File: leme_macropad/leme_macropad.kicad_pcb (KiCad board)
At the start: 4 copper layers, 99.9 x 63.9 mm, 90 parts, among them J1 OLED display, J2 USB_C_Receptacle_USB2.0_16P, SW1 SW_Push, SW2 SW_Push, SW3 SW_Push, SW4 RotaryEncoder_Switch, SW5 SW_Push, SW6 SW_Push, SW7 SW_Push, SW8 SW_Push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

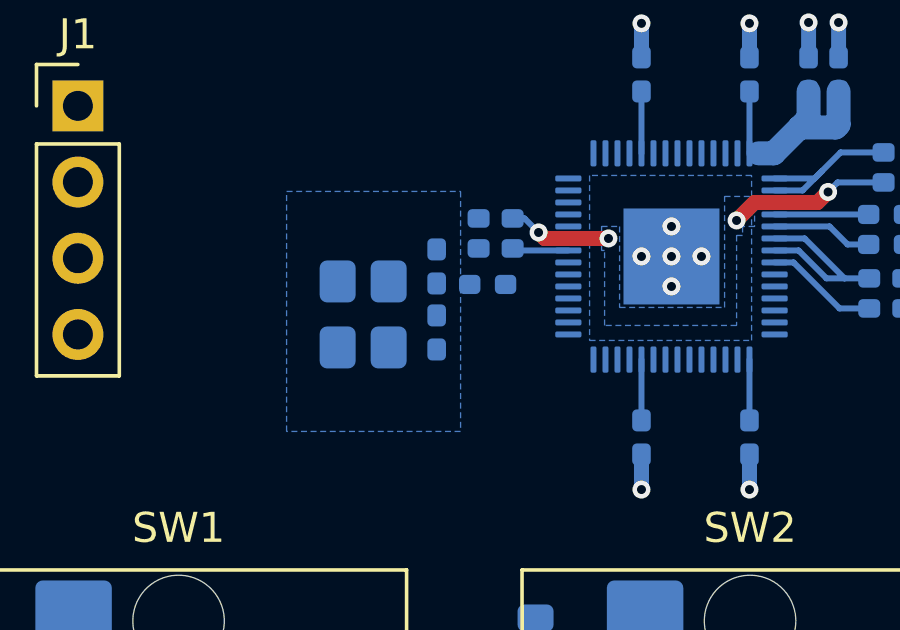
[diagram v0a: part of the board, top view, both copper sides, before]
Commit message: Routes crystal oscillator
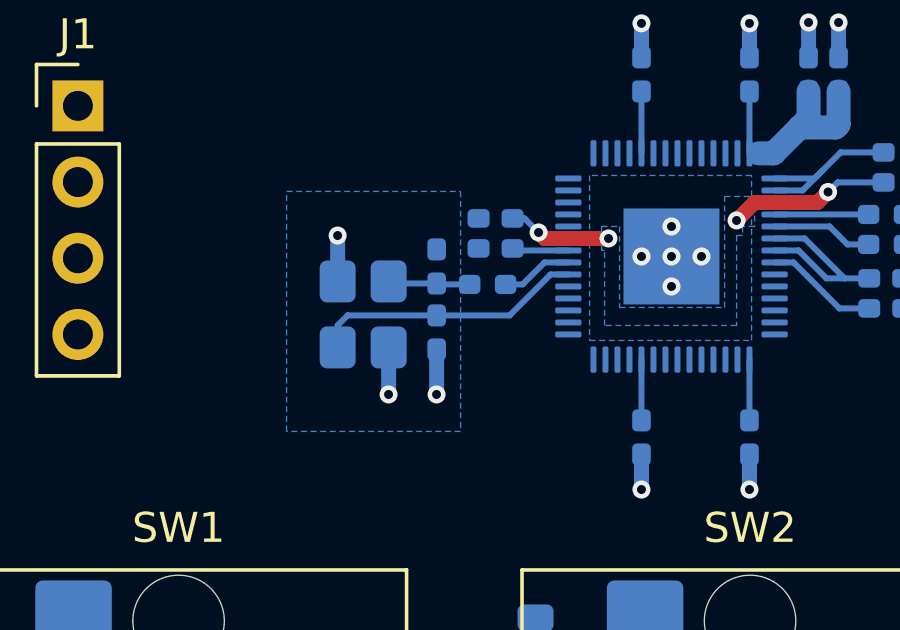
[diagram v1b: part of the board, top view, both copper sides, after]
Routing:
- net XIN: track 0.00 -> 9.13 mm
- net GND: track 12.8 -> 17.4 mm, vias 15 -> 18
- net Net-(C7-Pad2): track 0.00 -> 2.74 mm
- net XOUT: track 0.00 -> 2.40 mm
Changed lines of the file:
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@@
+	)
+	(via
+		(at 127.6 80)
+		(size 0.6)
+		(drill 0.3)
+		(layers "F.Cu" "B.Cu")
+		(net 2)
 	)
 	(via
@@
 	)
 	(via
+		(at 126 80)
+		(size 0.6)
+		(drill 0.3)
+		(layers "F.Cu" "B.Cu")
+		(net 2)
+	)
+	(via
+		(at 124.3025 74.7025)
+		(size 0.6)
+		(drill 0.3)
+		(layers "F.Cu" "B.Cu")
+		(net 2)
+	)
+	(via
 		(at 138.03 67.63)
 		(size 0.6)
@@
 		(drill 0.3)
 		(layers "F.Cu" "B.Cu")
+		(net 2)
+	)
+	(segment
+		(start 126.0025 79.9975)
+		(end 126 80)
+		(width 0.5)
+		(layer "B.Cu")
 		(net 2)
 	)
@@
 	)
 	(segment
+		(start 127.6025 79.9975)
+		(end 127.6 80)
+		(width 0.5)
+		(layer "B.Cu")
+		(net 2)
+	)
+	(segment
+		(start 126.0025 78.4325)
+		(end 126.0025 79.9975)
+		(width 0.5)
+		(layer "B.Cu")
+		(net 2)
+	)
+	(segment
 		(start 134.43 67.63)
 		(end 134.43 68.765)
@@
 	)
 	(segment
+		(start 124.3025 74.7025)
+		(end 124.3025 76.2325)
+		(width 0.5)
+		(layer "B.Cu")
+		(net 2)
+	)
+	(segment
 		(start 144.6 77.1325)
 		(end 143.157144 77.1325)
+		(width 0.5)
+		(layer "B.Cu")
+		(net 2)
+	)
+	(segment
+		(start 127.6025 78.5)
+		(end 127.6025 79.9975)
 		(width 0.5)
 		(layer "B.Cu")
@@
 	)
 	(segment
+		(start 124.635 77.365)
+		(end 127.6025 77.365)
+		(width 0.2)
+		(layer "B.Cu")
+		(net 4)
+	)
+	(segment
+		(start 131.4 76)
+		(end 131.9925 76)
+		(width 0.2)
+		(layer "B.Cu")
+		(net 4)
+	)
+	(segment
+		(start 127.6025 77.365)
+		(end 130.035 77.365)
+		(width 0.2)
+		(layer "B.Cu")
+		(net 4)
+	)
+	(segment
+		(start 124.3025 78.4325)
+		(end 124.3025 77.6975)
+		(width 0.2)
+		(layer "B.Cu")
+		(net 4)
+	)
+	(segment
+		(start 124.3025 77.6975)
+		(end 124.635 77.365)
+		(width 0.2)
+		(layer "B.Cu")
+		(net 4)
+	)
+	(segment
+		(start 130.035 77.365)
+		(end 131.4 76)
+		(width 0.2)
+		(layer "B.Cu")
+		(net 4)
+	)
+	(segment
+		(start 127.6025 76.3)
+		(end 126.07 76.3)
+		(width 0.2)
+		(layer "B.Cu")
+		(net 5)
+	)
+	(segment
+		(start 127.635 76.3325)
+		(end 127.6025 76.3)
+		(width 0.2)
+		(layer "B.Cu")
+		(net 5)
+	)
+	(segment
+		(start 126.07 76.3)
+		(end 126.0025 76.2325)
+		(width 0.2)
+		(layer "B.Cu")
+		(net 5)
+	)
+	(segment
+		(start 128.705 76.3325)
+		(end 127.635 76.3325)
+		(width 0.2)
+		(layer "B.Cu")
+		(net 5)
+	)
+	(segment
 		(start 140.65 73.25)
 		(end 140.3 73.6)
@@
 	)
 	(segment
+		(start 130.4675 76.3325)
+		(end 129.9 76.3325)
+		(width 0.2)
+		(layer "B.Cu")
+		(net 33)
+	)
+	(segment
+		(start 131.9925 75.6)
+		(end 131.2 75.6)
+		(width 0.2)
+		(layer "B.Cu")
+		(net 33)
+	)
+	(segment
+		(start 131.2 75.6)
+		(end 130.4675 76.3325)
+		(width 0.2)
+		(layer "B.Cu")
+		(net 33)
+	)
+	(segment

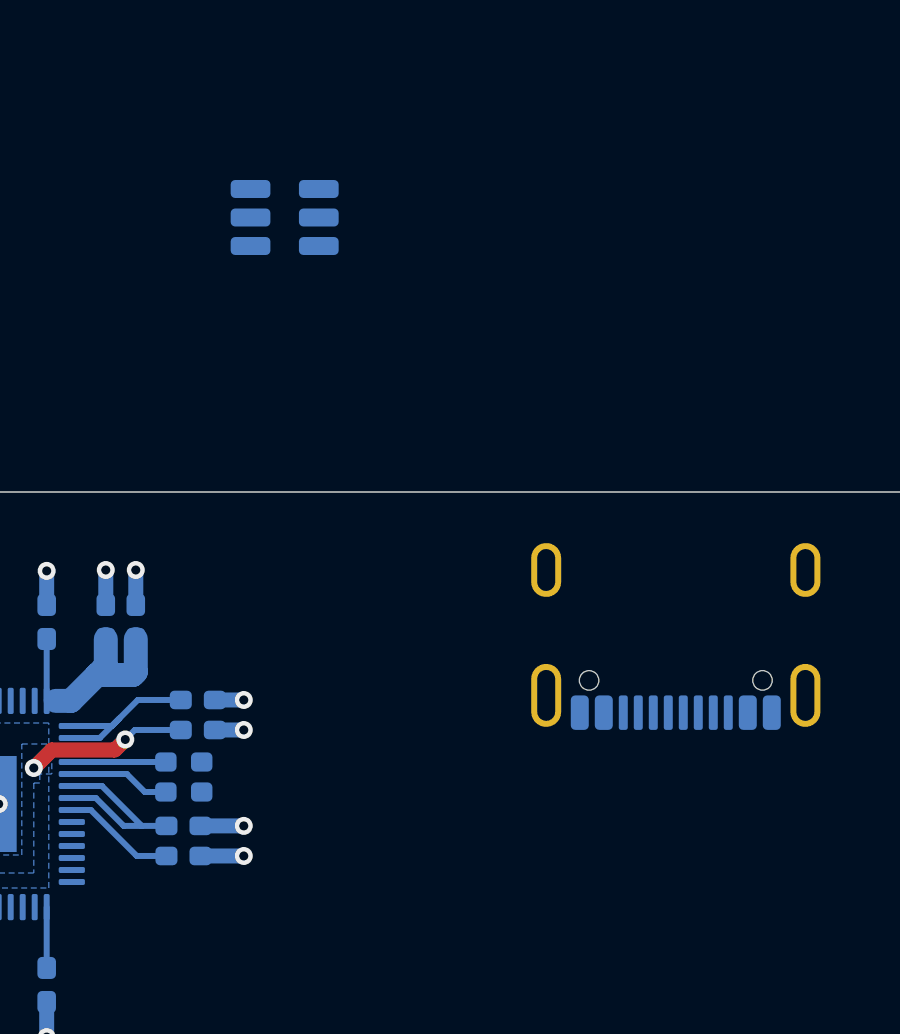
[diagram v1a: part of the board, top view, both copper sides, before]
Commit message: Routes USB diffpair
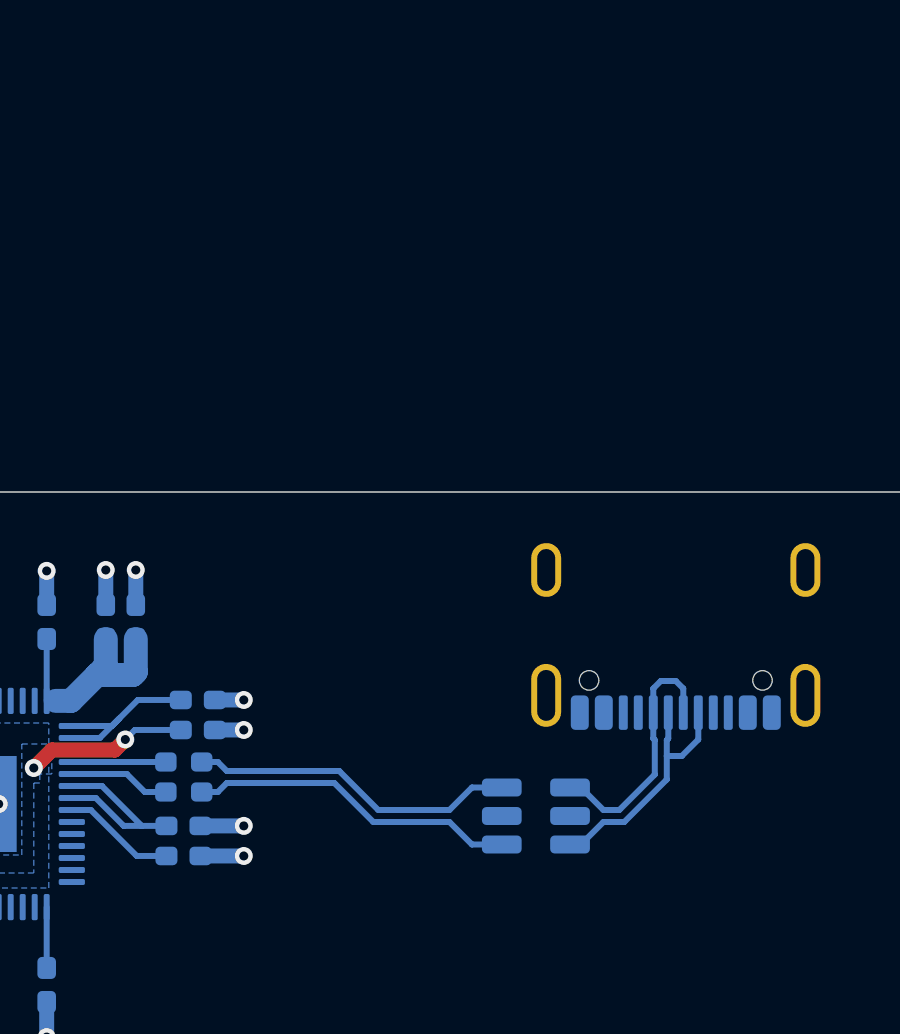
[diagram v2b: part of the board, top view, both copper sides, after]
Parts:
- moved U1 21.6 mm to (154.3, 75.8), turned to 180 degrees
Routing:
- net USB_D-: track 0.00 -> 11.0 mm
- net USB_D+: track 0.00 -> 11.0 mm
- net /conn_D+: track 0.00 -> 8.54 mm
- net /conn_D-: track 0.00 -> 8.53 mm

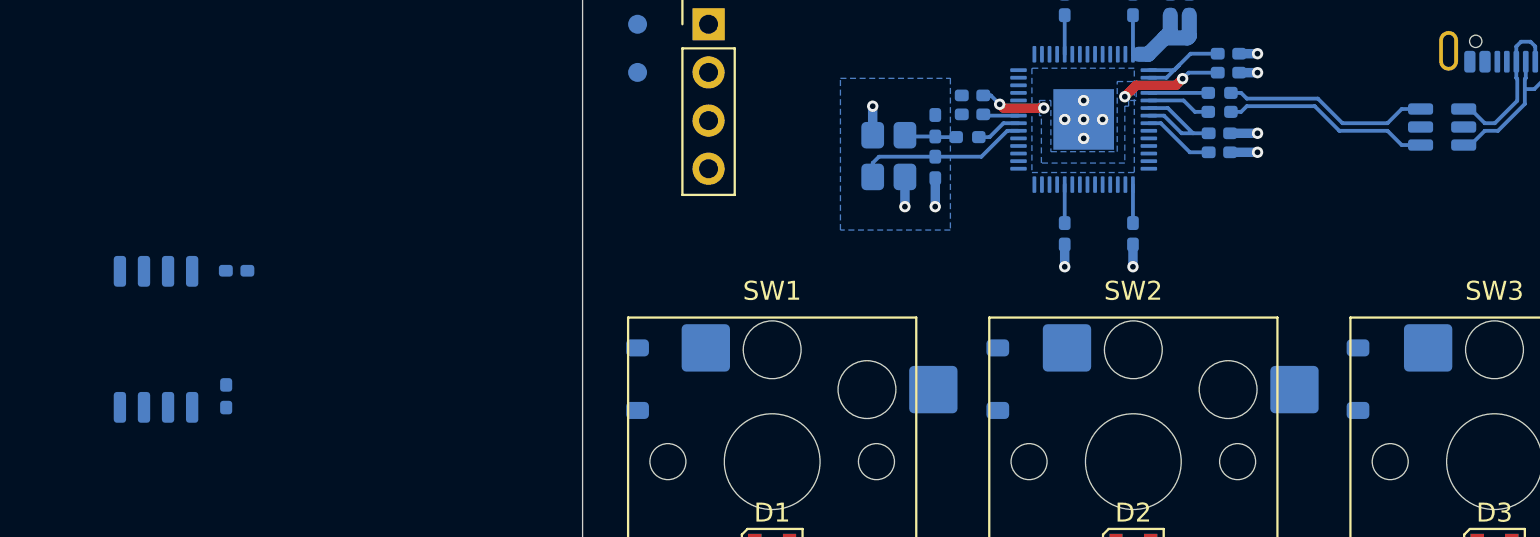
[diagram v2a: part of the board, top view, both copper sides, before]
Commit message: Routes QSPI data lines
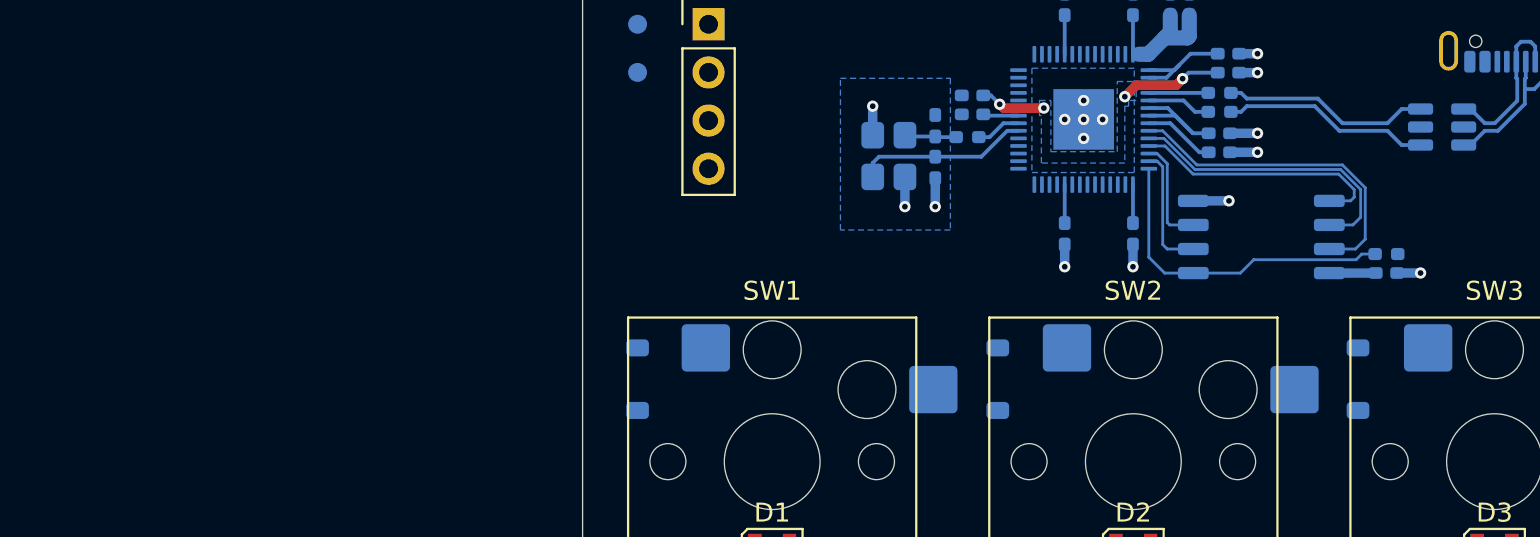
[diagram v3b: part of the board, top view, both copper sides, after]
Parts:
- moved R3 61.7 mm to (151.4, 82.5), turned to 0 degrees
- moved C0 60.7 mm to (151.4, 83.5)
- moved U0 58.5 mm to (144.8, 81.6), turned to 0 degrees
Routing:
- net QSPI_SD3: track 0.00 -> 17.5 mm
- net QSPI_SS: track 0.00 -> 17.4 mm
- net QSPI_SCLK: track 0.00 -> 15.6 mm
- net QSPI_SD0: track 0.00 -> 13.6 mm
- net QSPI_SD1: track 0.00 -> 6.67 mm
- net QSPI_SD2: track 0.00 -> 5.72 mm
- net GND: track 17.4 -> 20.5 mm, vias 18 -> 20
- net +3.3V: track 27.8 -> 30.3 mm

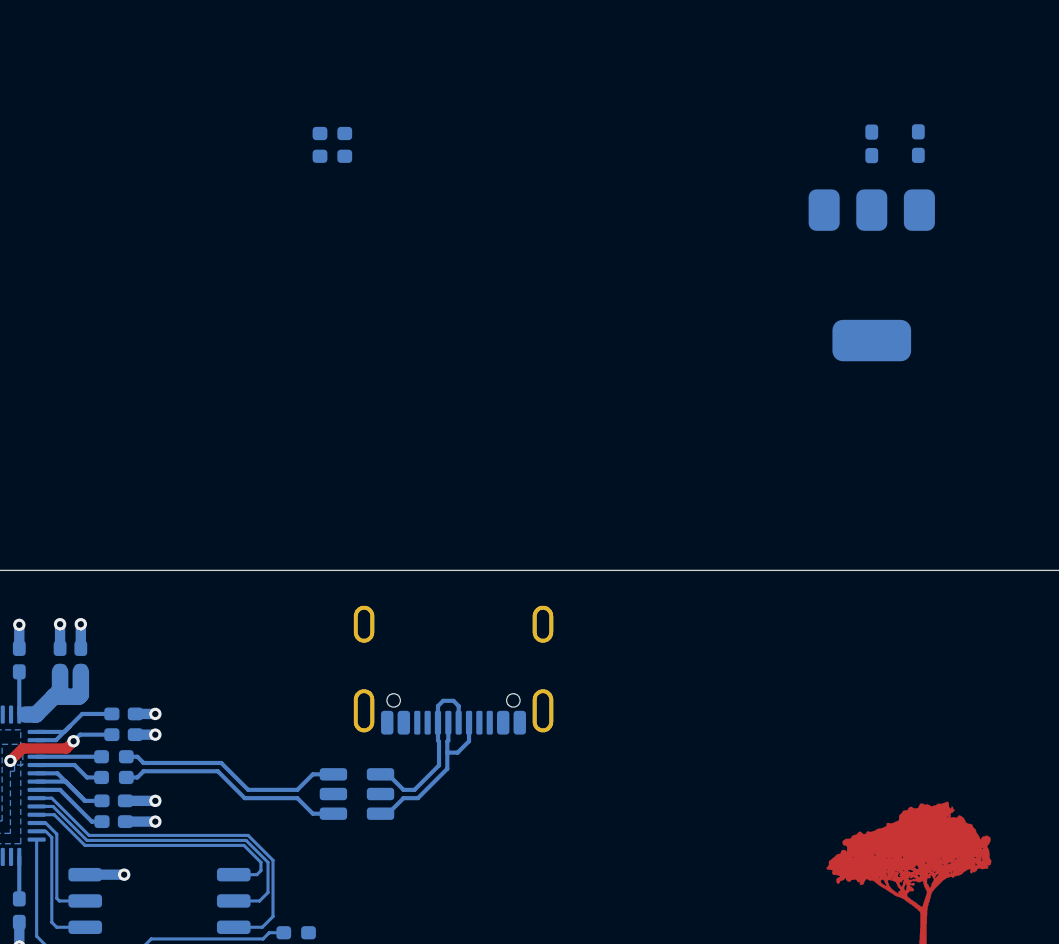
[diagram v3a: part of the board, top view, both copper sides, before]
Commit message: Moves USB connector to allow for more space for the power regulator
The connector was in the midpoint of the board (considering the
right-most part of the knob). Now it's a bit offset to the right.
This is less than ideal, but will make life much easier.
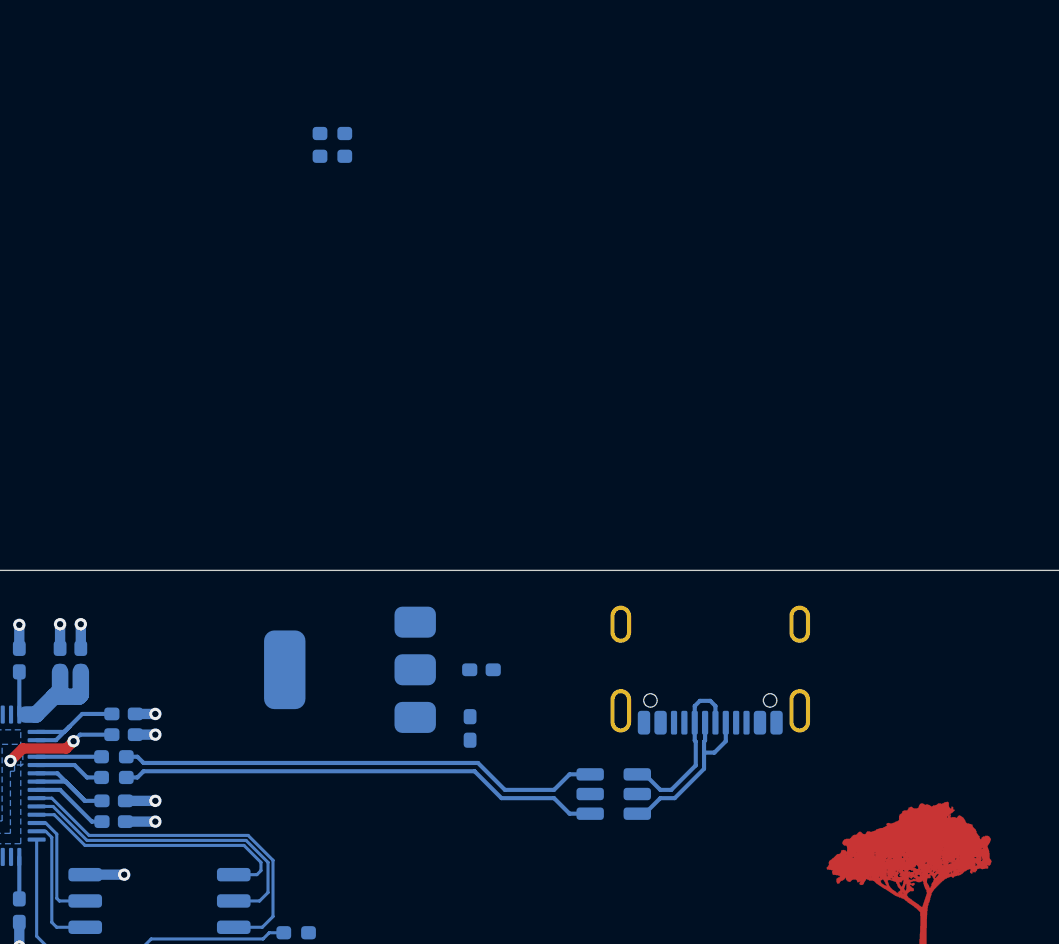
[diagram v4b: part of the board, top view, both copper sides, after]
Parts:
- moved C6 35.6 mm to (159.8, 72.6), turned to -90 degrees
- moved C8 31.6 mm to (160.3, 69.8), turned to 0 degrees
- moved U2 31.6 mm to (154.0, 69.8), turned to 180 degrees
- moved J2 12.4 mm to (171.4, 68.7)
- moved U1 12.4 mm to (166.7, 75.8)
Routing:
- net USB_D+: track 11.0 -> 23.4 mm
- net USB_D-: track 11.0 -> 23.4 mm

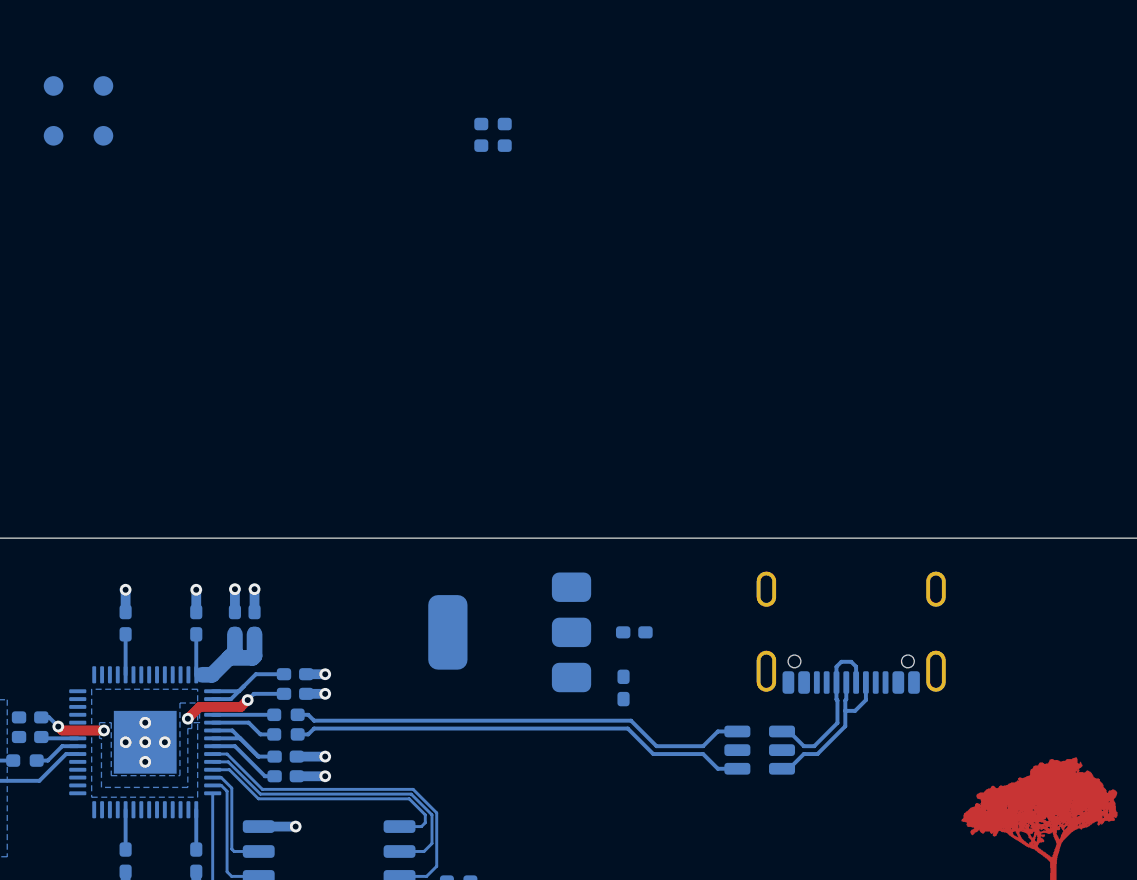
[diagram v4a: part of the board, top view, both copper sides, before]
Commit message: Routes power regulator
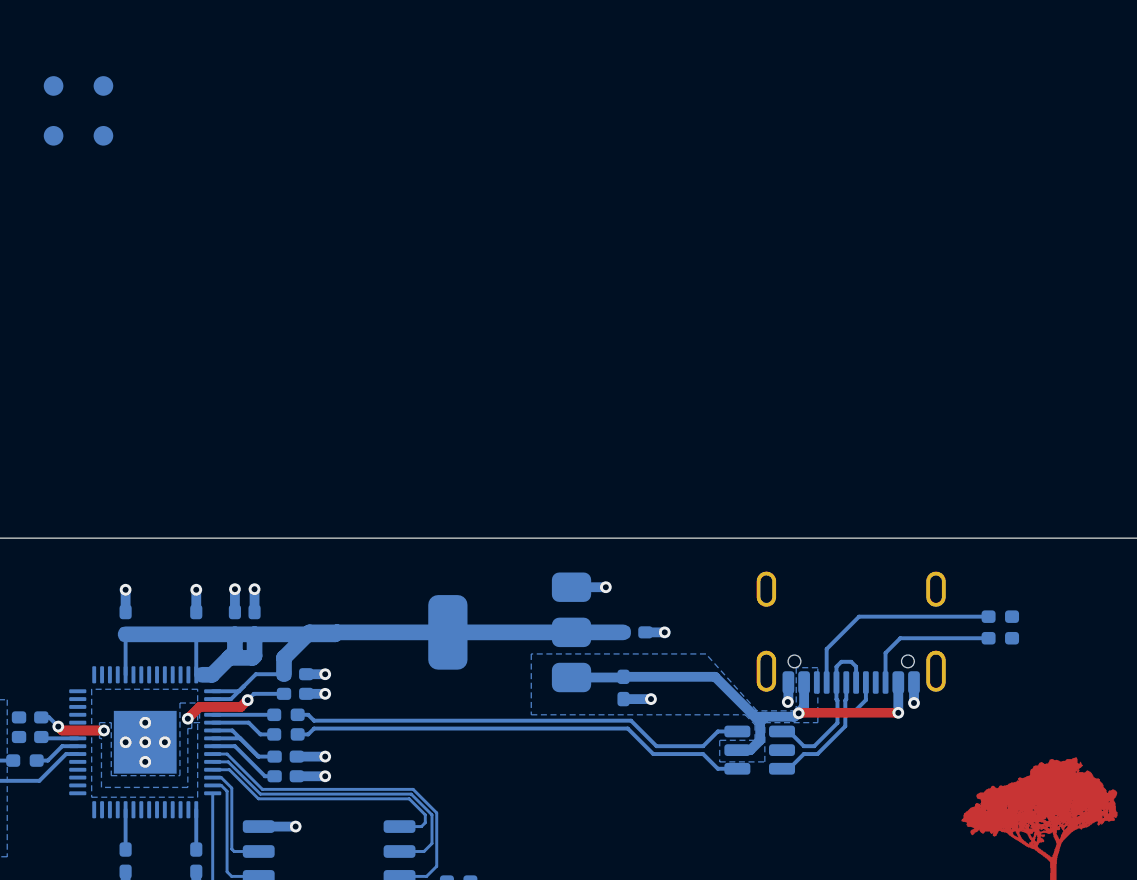
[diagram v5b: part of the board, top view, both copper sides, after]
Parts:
- moved R2 36.8 mm to (179.0, 70.1), turned to 0 degrees
- moved R4 35.3 mm to (179.0, 69.0), turned to 0 degrees
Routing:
- net +3.3V: track 30.3 -> 59.7 mm
- net +5V: track 0.00 -> 24.0 mm, vias 0 -> 2
- net Net-(J1-CC1): track 0.00 -> 10.6 mm
- net Net-(J1-CC2): track 0.00 -> 7.07 mm
- net GND: track 20.5 -> 26.7 mm, vias 20 -> 25
- added copper zone on B.Cu, net +5V
